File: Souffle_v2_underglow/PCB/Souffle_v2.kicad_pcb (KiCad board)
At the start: 2 copper layers, 137.2 x 109.2 mm, 88 parts, among them J1 LED, J2 4PIN, J3 OLED, SW1 SW_PUSH, SW10 SW_PUSH, SW11 SW_PUSH, SW12 SW_PUSH, SW13 SW_PUSH, SW14 SW_PUSH, SW15 SW_PUSH, SW16 SW_PUSH, SW17 SW_PUSH, SW18 SW_PUSH, SW19 SW_PUSH, SW2 SW_PUSH, SW20 SW_PUSH, SW21 SW_PUSH, SW22 SW_PUSH, SW23 SW_PUSH, SW24 SW_PUSH, SW25 SW_PUSH, SW25b1 RotaryEncoder_Switch, SW26 SW_PUSH, SW27 SW_PUSH, SW28 SW_PUSH, SW29 SW_PUSH, SW3 SW_PUSH, SW30 SW_PUSH, SW4 SW_PUSH, SW5 SW_PUSH, SW6 SW_PUSH, SW7 SW_PUSH, SW8 SW_PUSH, SW9 SW_PUSH, U1 ProMicro

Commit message: Checkpoint commit.
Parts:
- moved D34 131.6 mm to (189.1, 125.8), turned to 90 degrees
- moved D33 85.8 mm to (144.2, 107.3)
- moved D32 48.8 mm to (101.8, 115.9), turned to -90 degrees
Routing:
- net VCC: track 95.2 -> 187.5 mm, vias 3 -> 7
- net Net-(D32-Pad2): track 0.00 -> 60.6 mm, vias 0 -> 4
- net Net-(D31-Pad2): track 6.89 -> 48.9 mm, vias 1 -> 4
- net Net-(D33-Pad2): track 0.00 -> 6.20 mm, vias 0 -> 1
- net row4: track 172.3 -> 174.2 mm

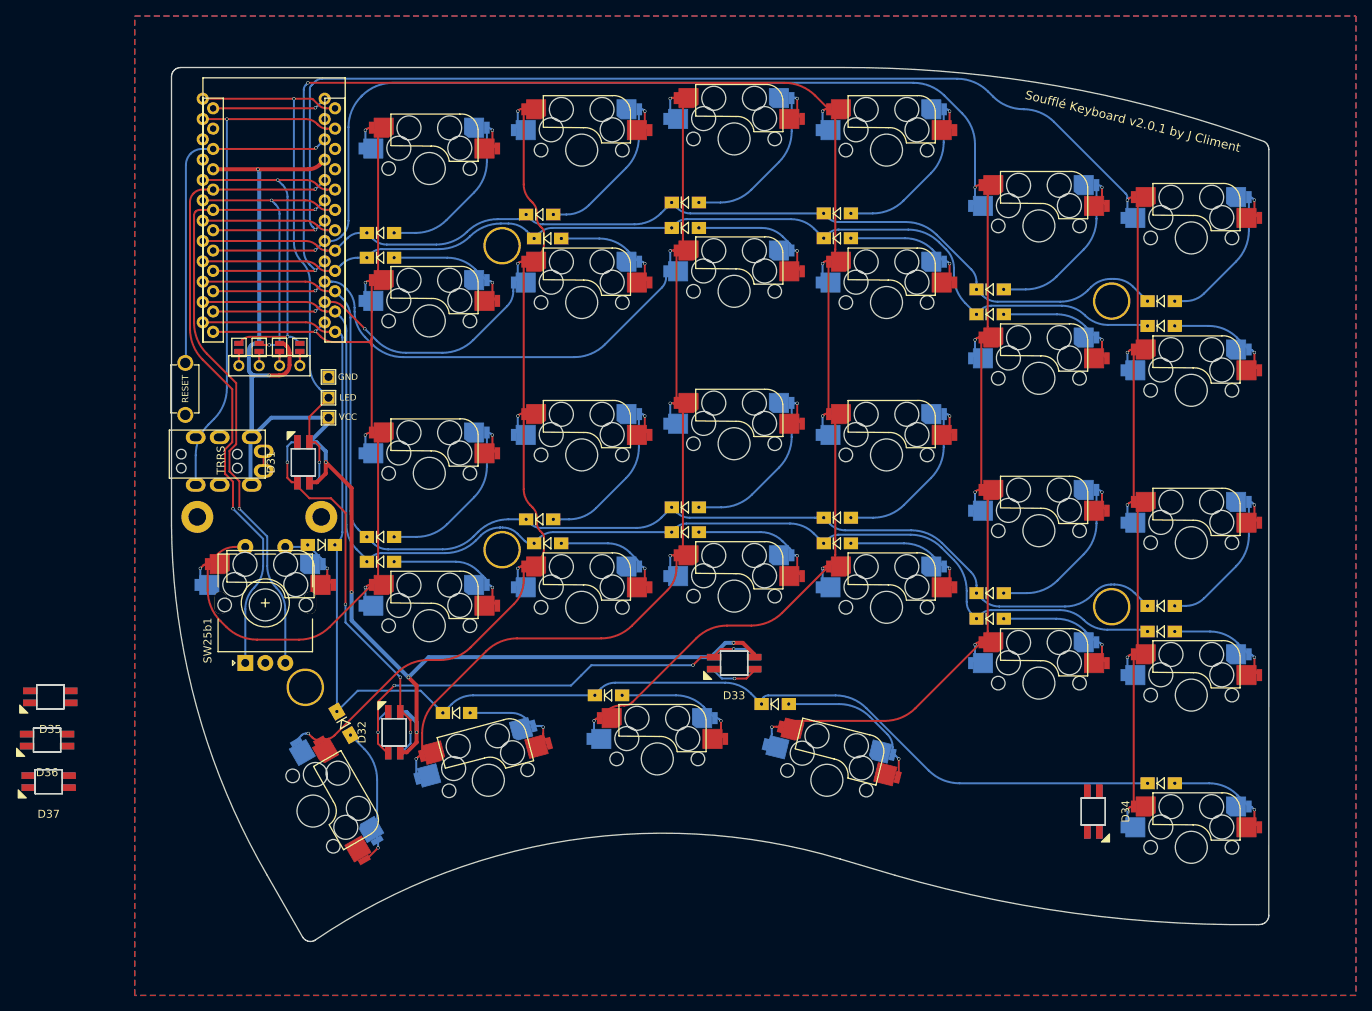
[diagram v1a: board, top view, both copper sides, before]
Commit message: LED placement and VCC pad for electricity supply to LEDs.
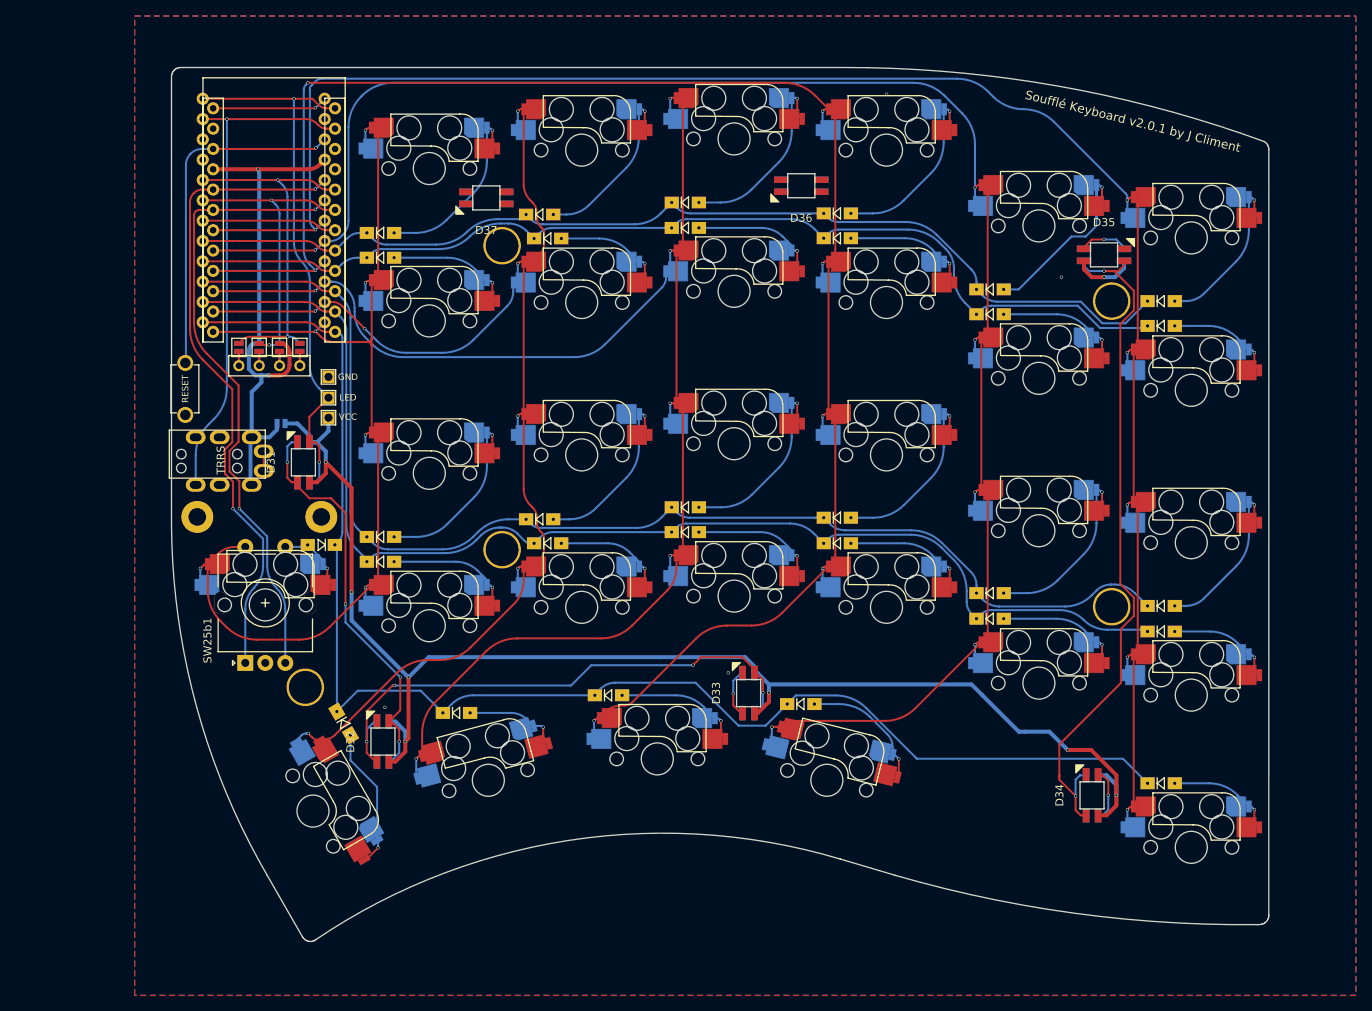
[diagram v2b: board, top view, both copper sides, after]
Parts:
- added JP9: SolderJumper_2_Open, footprints:Jumper, B.Cu at (87.6, 77.3)
- moved D35 142.8 mm to (190.5, 56.2), turned to 180 degrees
- moved D36 117.0 mm to (152.6, 47.6)
- moved D37 91.2 mm to (113.3, 49.1)
- moved D33 4.16 mm to (146.1, 111.0), turned to -90 degrees
- moved D29 3.21 mm to (152.6, 112.4)
- moved D34 2.03 mm to (189.0, 123.8), turned to -90 degrees
- moved D32 1.83 mm to (100.3, 117.1)
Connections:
- D31 pad 1: VCC -> LEDVCC
- D32 pad 1: VCC -> LEDVCC
- D33 pad 1: VCC -> LEDVCC
- D34 pad 1: VCC -> LEDVCC
- D35 pad 1: VCC -> LEDVCC
- D36 pad 1: VCC -> LEDVCC
- D37 pad 1: VCC -> LEDVCC
- J1 pad 1: VCC -> LEDVCC
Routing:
- net LEDVCC: track 0.00 -> 183.1 mm, vias 0 -> 8
- net VCC: track 187.5 -> 68.7 mm, vias 7 -> 2
- net Net-(D34-Pad2): track 0.00 -> 88.0 mm, vias 0 -> 2
- net Net-(D32-Pad2): track 60.6 -> 68.6 mm
- net Net-(D33-Pad2): track 6.20 -> 12.9 mm, vias 1 -> 2
- net Net-(D35-Pad2): track 0.00 -> 6.20 mm, vias 0 -> 1
- net Net-(D5-Pad2): track 23.5 -> 27.4 mm
- net Net-(D29-Pad2): track 19.6 -> 16.4 mm
- net row4: track 174.2 -> 177.0 mm
- net Net-(D31-Pad2): track 48.9 -> 50.7 mm
- net row1: track 128.7 -> 129.5 mm
- net GND: vias 0 -> 4

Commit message: More underglow changes.
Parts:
- moved D36 1.80 mm to (152.9, 45.8), turned to 180 degrees
- moved D34 1.02 mm to (190.0, 123.8), turned to 90 degrees
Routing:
- net Net-(D33-Pad2): track 12.9 -> 62.6 mm, vias 2 -> 4
- net Net-(D35-Pad2): track 6.20 -> 49.4 mm, vias 1 -> 6
- net Net-(D36-Pad2): track 0.00 -> 13.0 mm, vias 0 -> 2
- net LEDVCC: track 183.1 -> 191.9 mm, vias 8 -> 10
- net Net-(D1-Pad2): track 23.5 -> 29.2 mm
- net Net-(D34-Pad2): track 88.0 -> 83.5 mm
- net Net-(D5-Pad2): track 27.4 -> 23.4 mm
- net Net-(D3-Pad2): track 23.6 -> 24.9 mm
- net GND: vias 4 -> 5

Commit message: Checkpoint commit.
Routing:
- net LEDVCC: track 191.9 -> 312.3 mm, vias 10 -> 19
- net Net-(D36-Pad2): track 13.0 -> 49.0 mm, vias 2 -> 5
